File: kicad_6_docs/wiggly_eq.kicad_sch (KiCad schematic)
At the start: 7 parts, among them J1 audio_in, J2 audio_out, SW1 SW_3PDT_x3, U1 NE5532

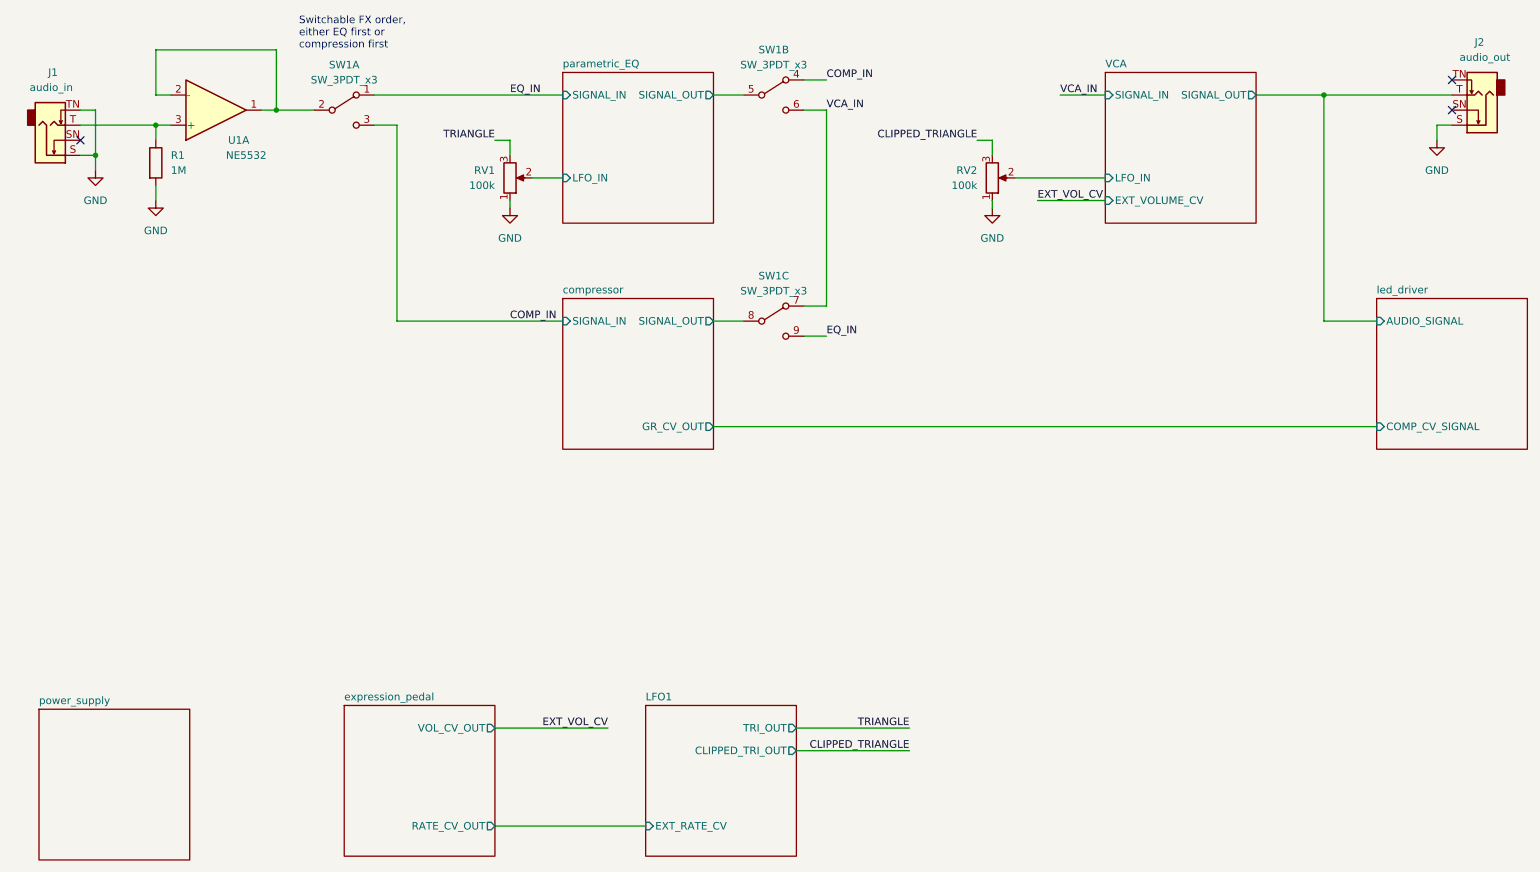
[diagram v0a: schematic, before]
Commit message: Fix power supply errors, tidy up schematic
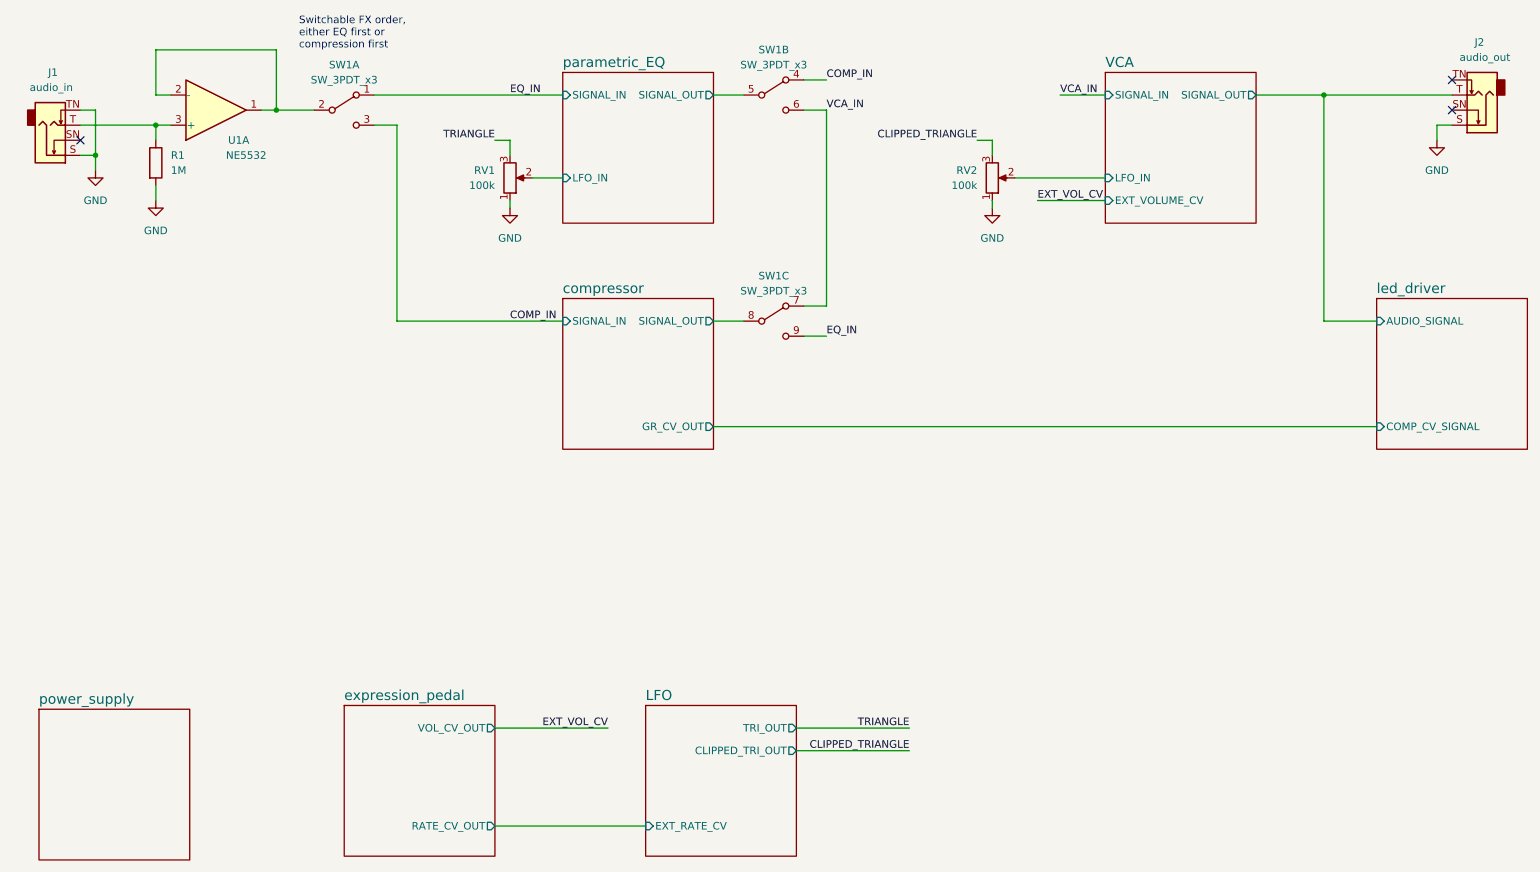
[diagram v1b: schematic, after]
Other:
- sheet LFO1 renamed LFO
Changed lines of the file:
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@@
   (title_block
     (title "Wiggly EQ")
-    (date "2022-05-29")
+    (date "2022-08-01")
     (rev "0")
     (comment 2 "creativecommons.org/licenses/by/4.0")
@@
     (fill (color 0 0 0 0.0000))
     (property "Sheet name" "VCA" (id 0) (at 204.47 57.7084 0)
-      (effects (font (size 1.27 1.27)) (justify left bottom))
+      (effects (font (size 1.7 1.7)) (justify left bottom))
     )
     (property "Sheet file" "VCA.kicad_sch" (id 1) (at 204.47 84.4046 0)
@@
     (fill (color 0 0 0 0.0000))
     (property "Sheet name" "power_supply" (id 0) (at 24.765 165.0234 0)
-      (effects (font (size 1.27 1.27)) (justify left bottom))
+      (effects (font (size 1.7 1.7)) (justify left bottom))
     )
     (property "Sheet file" "power_supply.kicad_sch" (id 1) (at 24.765 191.7196 0)
@@
     (fill (color 0 0 0 0.0000))
     (property "Sheet name" "compressor" (id 0) (at 113.03 95.8084 0)
-      (effects (font (size 1.27 1.27)) (justify left bottom))
+      (effects (font (size 1.7 1.7)) (justify left bottom))
     )
     (property "Sheet file" "compressor.kicad_sch" (id 1) (at 113.03 122.5046 0)
@@
     (fill (color 0 0 0 0.0000))
     (property "Sheet name" "expression_pedal" (id 0) (at 76.2 164.3884 0)
-      (effects (font (size 1.27 1.27)) (justify left bottom))
+      (effects (font (size 1.7 1.7)) (justify left bottom))
     )
     (property "Sheet file" "expression_pedal.kicad_sch" (id 1) (at 76.2 191.0846 0)
@@
     (fill (color 0 0 0 0.0000))
     (property "Sheet name" "led_driver" (id 0) (at 250.19 95.8084 0)
-      (effects (font (size 1.27 1.27)) (justify left bottom))
+      (effects (font (size 1.7 1.7)) (justify left bottom))
     )
     (property "Sheet file" "led_driver.kicad_sch" (id 1) (at 250.19 122.5046 0)
@@
     (fill (color 0 0 0 0.0000))
     (property "Sheet name" "parametric_EQ" (id 0) (at 113.03 57.7084 0)
-      (effects (font (size 1.27 1.27)) (justify left bottom))
+      (effects (font (size 1.7 1.7)) (justify left bottom))
     )
     (property "Sheet file" "parametric_EQ.kicad_sch" (id 1) (at 113.03 84.4046 0)
@@
     (stroke (width 0.1524) (type solid) (color 0 0 0 0))
     (fill (color 0 0 0 0.0000))
-    (property "Sheet name" "LFO1" (id 0) (at 127 164.3884 0)
-      (effects (font (size 1.27 1.27)) (justify left bottom))
+    (property "Sheet name" "LFO" (id 0) (at 127 164.3884 0)
+      (effects (font (size 1.7 1.7)) (justify left bottom))
     )
     (property "Sheet file" "LFO.kicad_sch" (id 1) (at 127 191.0846 0)
